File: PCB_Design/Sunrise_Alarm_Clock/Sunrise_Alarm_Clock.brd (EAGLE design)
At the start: 101.6 x 69.5 mm, 25 parts, among them T1 2N3904, T2 2N3904, T3 2N3904, T4 2N3904

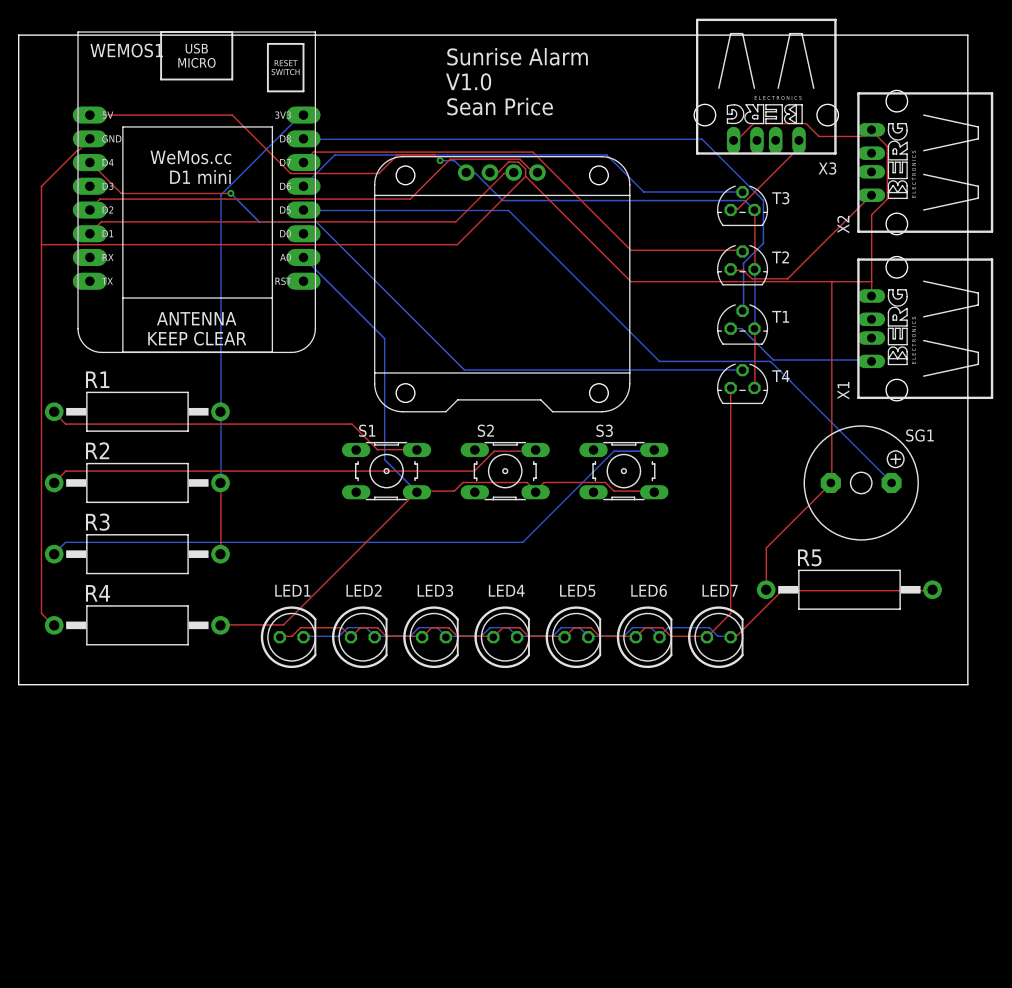
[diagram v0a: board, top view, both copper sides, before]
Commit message: V2.1.1-alpha PCB V1.1
- Placed LEDs, USBs and D1 mini on the rear of the board
- Changed USB footprint to include shield pads
- Fixed transistors to be common-emitter
- Broke schematic into sections to make it easier to follow
- Hand-routed thicker traces
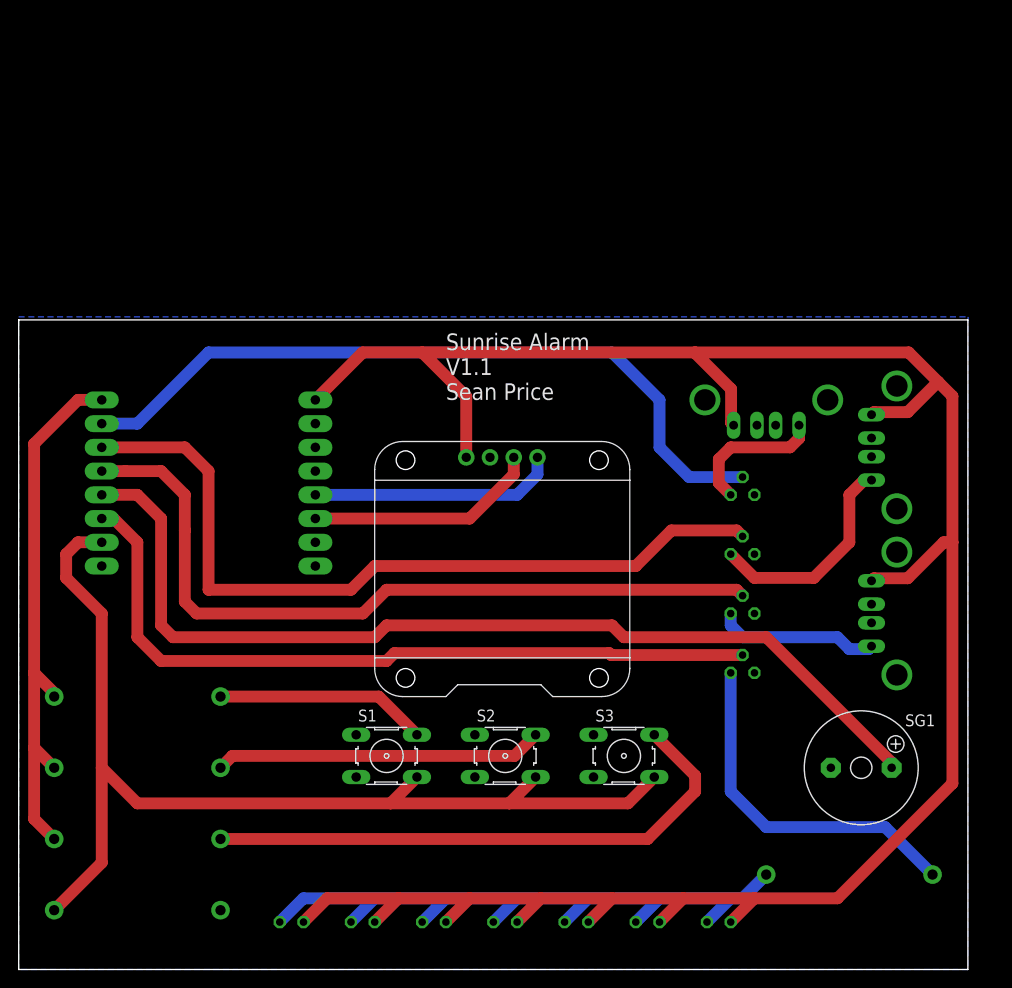
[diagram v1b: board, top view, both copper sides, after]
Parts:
- X1, X2, X3: value (none) -> PN87520-S; device con-berg:PN87520 -> con-berg:PN87520-S
- moved WEMOS1 30.5 mm to (19.1, 50.8), flipped to the bottom
- moved LED1 30.5 mm to (29.2, 5.08), flipped to the bottom
- moved LED2 30.5 mm to (36.8, 5.08), flipped to the bottom
- moved LED3 30.5 mm to (44.5, 5.08), flipped to the bottom
- moved LED4 30.5 mm to (52.1, 5.08), flipped to the bottom
- moved LED5 30.5 mm to (59.7, 5.08), flipped to the bottom
- moved LED6 30.5 mm to (67.3, 5.08), flipped to the bottom
- moved LED7 30.5 mm to (74.9, 5.08), flipped to the bottom
- moved R3 30.5 mm to (12.7, 14.0), flipped to the bottom
- moved S1 30.5 mm to (39.4, 22.9)
- moved S2 30.5 mm to (52.1, 22.9)
- moved S3 30.5 mm to (64.8, 22.9)
- moved T2 30.5 mm to (77.5, 44.5), flipped to the bottom
- moved T3 30.5 mm to (77.5, 50.8), flipped to the bottom
- moved R2 30.5 mm to (12.7, 21.6), flipped to the bottom
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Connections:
- net N$10 renamed A0
- net N$12 renamed 3V3
- net N$15 renamed D5
- net N$17 renamed D7
- net N$3 renamed SCL
- net N$4 renamed SDA
- removed net N$13: T3.2, WEMOS1.D6
- removed net N$16: T1.2, WEMOS1.D8
- removed net N$19: LED1.A, LED2.A, LED3.A, LED4.A, LED5.A, LED6.A, LED7.A, T4.3
- removed net N$2: R4.1, R5.1, SG1.-, U$1.GND, WEMOS1.GND, X1.4, X2.4, X3.4
- removed net N$20: T4.2, WEMOS1.D4
- removed net N$7: T3.3, X3.1
- new net D0: T4.2, WEMOS1.D0
- new net D6: T1.2, WEMOS1.D6
- new net D8: T3.2, WEMOS1.D8
- new net GND: R4.1, SG1.-, T1.3, T2.3, T3.3, T4.3, U$1.GND, WEMOS1.GND
- new net N$14: R5.1, T4.1
- new net VCC: LED1.A, LED2.A, LED3.A, LED4.A, LED5.A, LED6.A, LED7.A, U$1.VCC, WEMOS1.5V, X1.1, X2.1, X3.1
- net N$1: now also X3.4; no longer T1.1, T2.1, T4.1, U$1.VCC, WEMOS1.5V
- net N$5: now also T2.1, X2.4; no longer T1.3, X1.1
- net N$6: now also T1.1, X1.4; no longer T2.3, X2.1
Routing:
- net VCC: track 0.00 -> 252.5 mm
- net N$2: track 228.3 -> 0.00 mm
- net D6: track 0.00 -> 82.9 mm
- net D0: track 0.00 -> 81.3 mm
- net N$1: track 96.2 -> 15.2 mm, vias 1 -> 0
- net D8: track 0.00 -> 80.2 mm
- net N$20: track 79.1 -> 0.00 mm, vias 1 -> 0
- net N$19: track 78.6 -> 0.00 mm
- net N$16: track 64.7 -> 0.00 mm
- net N$13: track 50.0 -> 0.00 mm
- net N$14: track 0.00 -> 38.0 mm
- net D7: track 51.9 -> 85.2 mm
- net A0: track 84.3 -> 116.0 mm
- net D5: track 75.1 -> 104.7 mm
- net SDA: track 50.8 -> 26.5 mm
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- added copper zone on layer 16, net GND
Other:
- board text added: "Sunrise Alarm V1.1 Sean Price"
- board text removed: "Sunrise Alarm V1.0 Sean Price"
